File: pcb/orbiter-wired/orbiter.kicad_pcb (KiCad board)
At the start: 2 copper layers, 140 x 91 mm, 144 parts, among them J1 SWD, J2 AudioJack4, J3 SWD, J4 AudioJack4, SW1 SW_SPDT, SW10 SW_Push, SW11 SW_Push, SW12 SW_Push, SW13 SW_Push, SW14 SW_Push, SW15 SW_Push, SW16 SW_Push, SW17 SW_Push, SW18 SW_Push, SW19 SW_Push, SW2 SW_Push, SW20 SW_Push, SW21 SW_Push, SW22 SW_Push, SW23 SW_Push, SW24 SW_Push, SW25 SW_Push, SW26 SW_Push, SW27 SW_Push, SW28 SW_SPDT, SW3 SW_Push, SW4 SW_Push, SW5 SW_Push, SW6 SW_Push, SW7 SW_Push, SW8 SW_Push, SW9 SW_Push, U1 TPS82140

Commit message: Change diode footprints 0603 -> SOD-323
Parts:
- D1, D10, D11, D12, D13, D14, D15, D16, D17, D18, D19, D2, D20, D21, D22, D23, D24, D25, D26, D27, D28, D29, D3, D30, D31, D32, D33, D34, D35, D36, D37, D38, D39, D4, D40, D41, D42, D43, D44, D45, D46, D47, D48, D49, D5, D50, D51, D52, D6, D7, D8, D9: footprint Diode:D_0603_1608Metric_Pad1.05x0.95mm_HandSolder -> Diode_SMD:D_SOD-323_HandSoldering
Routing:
- net Net-(D50-A): track 17.3 -> 18.0 mm
- net Net-(D42-A): track 17.6 -> 18.3 mm
- net Net-(D34-A): track 16.8 -> 17.4 mm

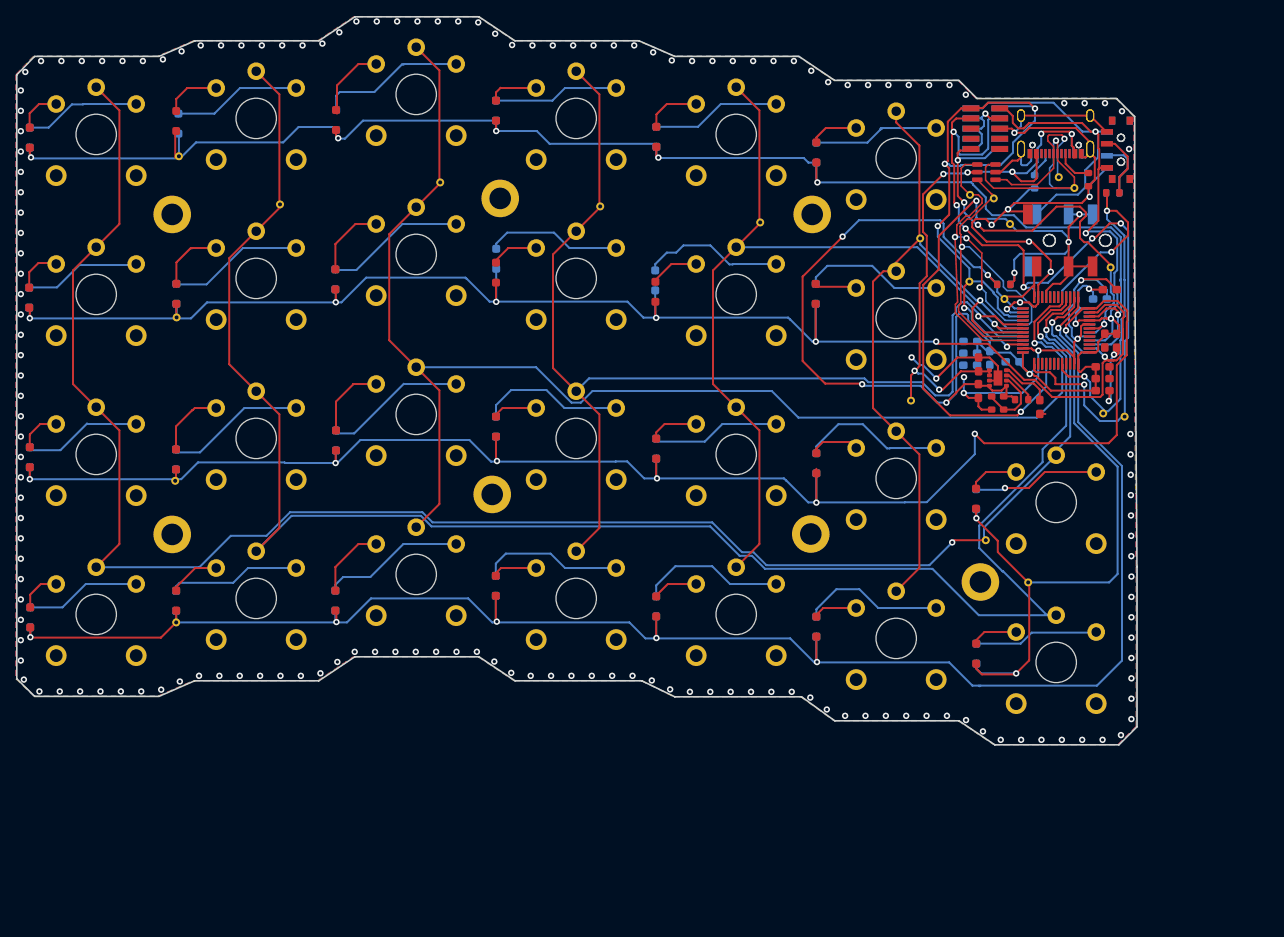
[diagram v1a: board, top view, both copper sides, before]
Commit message: Move symbols into their own folder
Add footprint and symbol for TPS82140SILR that is correct size
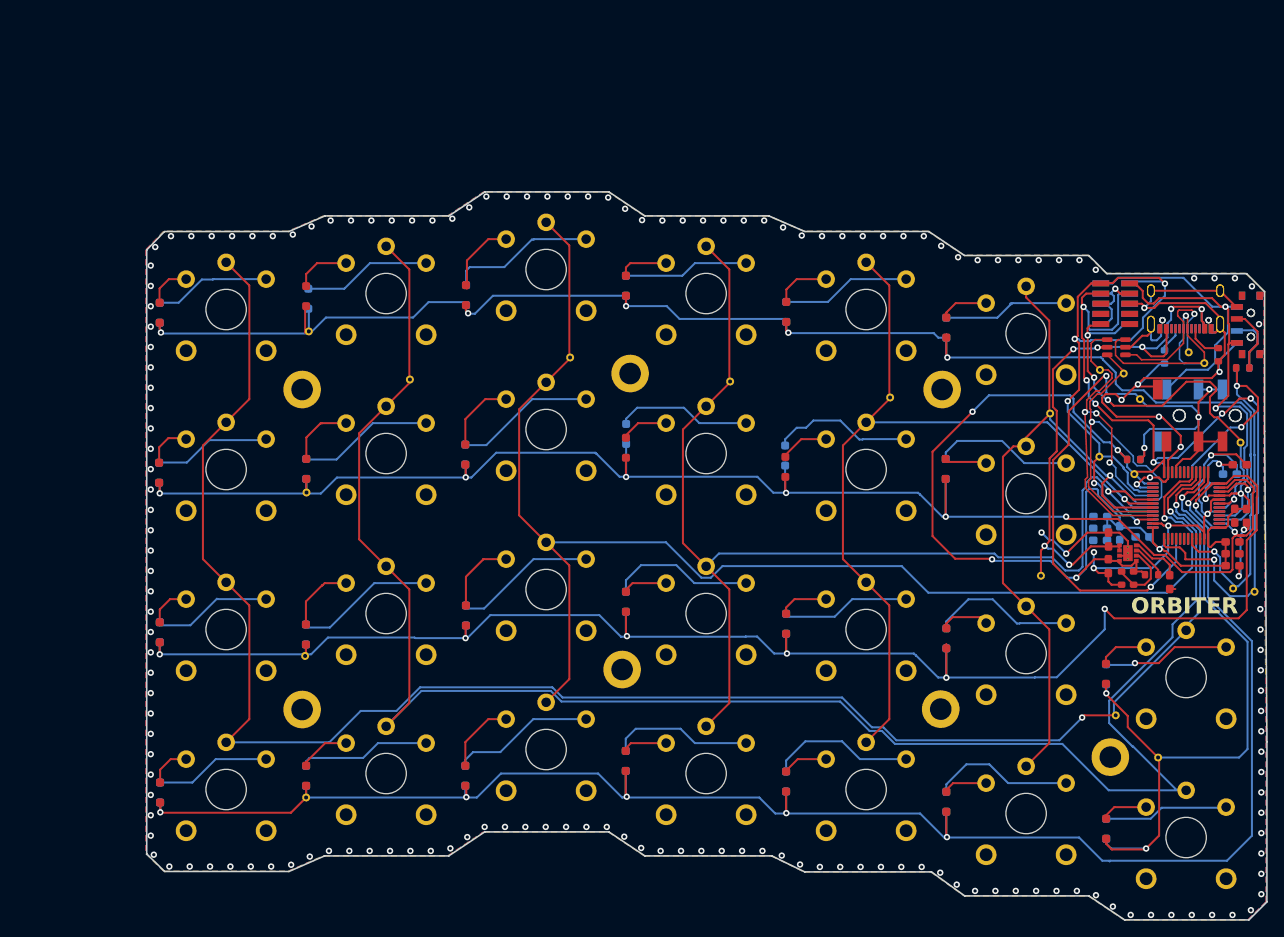
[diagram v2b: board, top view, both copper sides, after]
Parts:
- U1: value TPS82140 -> TPS82140SILR; footprint Package_LGA:Texas_SIL0008D_MicroSiP-8-1EP_2.8x3mm_P0.65mm_EP1.1x1.9mm -> TPS82140SILR:TPS82140SILR
- moved C13 27.3 mm to (205.5, 94.2)
- moved C17 27.3 mm to (205.5, 95.7)
- moved COL1 27.3 mm to (207.4, 117.6)
- moved D10 27.3 mm to (206.2, 112.5)
- moved D32 27.3 mm to (146.2, 123.3)
- moved D34 27.3 mm to (146.2, 82.4)
- moved D36 27.3 mm to (146.2, 123.3)
- moved D50 27.3 mm to (186.2, 86.8)
- moved R12 27.3 mm to (223.3, 74.2)
- moved R6 27.3 mm to (223.3, 74.2)
- moved USB_DP_TP1 27.3 mm to (205.5, 74.4)
- moved D12 27.3 mm to (106.3, 86.8)
- moved D17 27.3 mm to (106.3, 86.8)
- moved D19 27.3 mm to (106.2, 125.2)
- moved D29 27.3 mm to (146.2, 63.9)
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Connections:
- net /T_KEY_ROW0 renamed /T_MCU_ROW0
- net /T_KEY_ROW1 renamed /T_MCU_ROW1
- net /T_KEY_ROW2 renamed /T_MCU_ROW2
- net /T_KEY_ROW3 renamed /T_MCU_ROW3
- net /T_KEY_ROW4 renamed /T_MCU_ROW4
- net /VBUS renamed /TPS_EN
- net /VOUT_3V3 renamed /TPS_VOUT
- net Net-(U1-FB) renamed /TPS_FB
- net Net-(U1-PG) renamed /TPS_PG
- net Net-(U1-SS/TR) renamed /TPS_SS

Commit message: Put all diodes on respective side
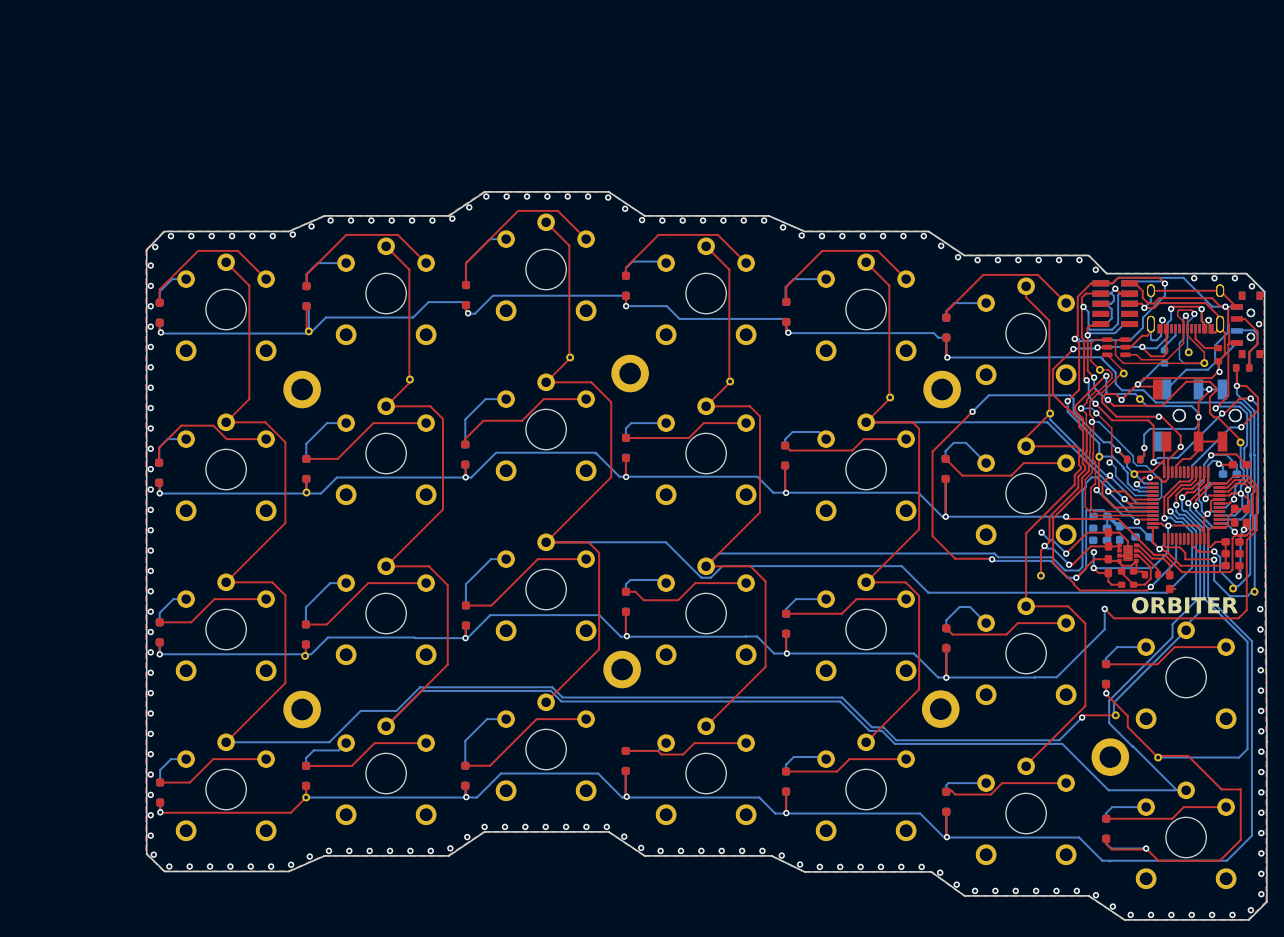
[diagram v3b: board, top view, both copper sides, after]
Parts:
- D1, D11, D12, D13, D14, D15, D2, D21, D22, D23, D24, D29, D3, D30, D31, D32, D37, D38, D39, D4, D40, D45, D46, D47, D48, D5: moved to B.Cu
- D10, D16, D17, D18, D19, D20, D25, D26, D27, D28, D33, D34, D35, D36, D41, D42, D43, D44, D49, D50, D51, D52, D6, D7, D8, D9: moved to F.Cu
- moved D34 1.76 mm to (146.2, 84.2)
- moved D38 1.43 mm to (166.1, 85.1)
- moved D16 0.38 mm to (106.3, 65.2)
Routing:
- net /T_MCU_ROW4: track 90.0 -> 109.6 mm
- net /T_MCU_COL1: track 227.5 -> 240.9 mm
- net /T_MCU_COL2: track 170.0 -> 183.5 mm
- net /T_MCU_COL0: track 223.2 -> 236.6 mm
- net /T_MCU_COL3: track 143.8 -> 157.2 mm
- net /T_MCU_COL5: track 95.9 -> 108.6 mm
- net /T_MCU_COL4: track 111.7 -> 124.2 mm
- net /TPS_VOUT: track 247.5 -> 242.9 mm
- net Net-(D41-A): track 16.3 -> 20.2 mm
- net Net-(D6-A): track 14.7 -> 18.4 mm
- net Net-(D33-A): track 15.8 -> 19.6 mm
- net Net-(D16-A): track 16.2 -> 19.9 mm
- net Net-(D49-A): track 16.0 -> 19.1 mm
- net Net-(D25-A): track 18.8 -> 21.9 mm
- net /TPS_EN: track 79.1 -> 82.2 mm
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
